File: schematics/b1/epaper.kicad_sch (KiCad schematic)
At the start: 0 parts

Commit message: Added schematic page for the status block.
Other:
- company: (none) -> shawnd.xyz
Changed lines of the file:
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@@
   (title_block
     (title "B1")
-    (date "2024-02-01")
+    (date "2024-02-05")
     (rev "1")
+    (company "shawnd.xyz")
     (comment 2 "scanning as well as radio communications and outputs/displays.")
     (comment 3 "A B1 (Badger One) node is the core hardware unit of the Badger sytem. It handles card")

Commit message: Added schematic page for e-paper block.
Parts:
- added C15: 10u, symbol Device:C_Polarized
- added C16: 1u, symbol Device:C
- added C17: 0.1u, symbol Device:C
- added U5: ~, symbol custom:E-paper_Display
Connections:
- new net BUSY: U5.1 (BUSY)
- new net CLK: U5.5 (CLK)
- new net CS: U5.4 (CS)
- new net DC: U5.3 (DC)
- new net DIN: U5.6 (DIN)
- new net GND: C15.2, C16.2, C17.2, U5.7 (GND)
- new net RST: U5.2 (RST)
- new net VCC: C15.1, C16.1, C17.1, U5.8 (VCC)
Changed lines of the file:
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@@
 (kicad_sch (version 20230121) (generator eeschema)
-  (paper "A4")
+  (paper "A5")
   (title_block
     (title "B1")
@@
     (rev "1")
     (company "shawnd.xyz")
-    (comment 2 "scanning as well as radio communications and outputs/displays.")
-    (comment 3 "A B1 (Badger One) node is the core hardware unit of the Badger sytem. It handles card")
+    (comment 3 "for text, images, or shapes.")
+    (comment 4 "The e-paper block is just a Waveshare 2.9-inch e-paper module that provides a display")
+  )
+  (junction (at 78.74 40.64) (diameter 0) (color 0 0 0 0)
+  )
+  (junction (at 66.04 50.8) (diameter 0) (color 0 0 0 0)
+  )
+  (junction (at 90.17 40.64) (diameter 0) (color 0 0 0 0)
+  )
+  (junction (at 104.14 40.64) (diameter 0) (color 0 0 0 0)
+  )
+  (junction (at 78.74 50.8) (diameter 0) (color 0 0 0 0)
+  )
+  (wire (pts (xy 90.17 40.64) (xy 90.17 41.91))
+    (stroke (width 0) (type default))
+  )
+  (wire (pts (xy 66.04 52.07) (xy 66.04 50.8))
+    (stroke (width 0) (type default))
+  )
+  (wire (pts (xy 78.74 50.8) (xy 78.74 49.53))
+    (stroke (width 0) (type default))
+  )
+  (wire (pts (xy 78.74 40.64) (xy 78.74 41.91))
+    (stroke (width 0) (type default))
+  )
+  (wire (pts (xy 66.04 49.53) (xy 66.04 50.8))
+    (stroke (width 0) (type default))
+  )
+  (wire (pts (xy 90.17 40.64) (xy 78.74 40.64))
+    (stroke (width 0) (type default))
+  )
+  (wire (pts (xy 104.14 50.8) (xy 104.14 40.64))
+    (stroke (width 0) (type default))
+  )
+  (wire (pts (xy 90.17 40.64) (xy 104.14 40.64))
+    (stroke (width 0) (type default))
+  )
+  (wire (pts (xy 104.14 39.37) (xy 104.14 40.64))
+    (stroke (width 0) (type default))
+  )
+  (wire (pts (xy 90.17 50.8) (xy 90.17 49.53))
+    (stroke (width 0) (type default))
+  )
+  (wire (pts (xy 66.04 41.91) (xy 66.04 40.64))
+    (stroke (width 0) (type default))
+  )
+  (wire (pts (xy 66.04 40.64) (xy 78.74 40.64))
+    (stroke (width 0) (type default))
+  )
+  (wire (pts (xy 78.74 50.8) (xy 90.17 50.8))
+    (stroke (width 0) (type default))
+  )
+  (wire (pts (xy 66.04 50.8) (xy 78.74 50.8))
+    (stroke (width 0) (type default))
+  )
+  (hierarchical_label "RST" (shape input) (at 93.98 58.42 180) (fields_autoplaced)
+    (effects (font (size 1.27 1.27)) (justify right))
+  )
+  (hierarchical_label "CLK" (shape input) (at 93.98 66.04 180) (fields_autoplaced)
+    (effects (font (size 1.27 1.27)) (justify right))
+  )
+  (hierarchical_label "DIN" (shape input) (at 93.98 68.58 180) (fields_autoplaced)
+    (effects (font (size 1.27 1.27)) (justify right))
+  )
+  (hierarchical_label "DC" (shape input) (at 93.98 60.96 180) (fields_autoplaced)
+    (effects (font (size 1.27 1.27)) (justify right))
+  )
+  (hierarchical_label "CS" (shape input) (at 93.98 63.5 180) (fields_autoplaced)
+    (effects (font (size 1.27 1.27)) (justify right))
+  )
+  (hierarchical_label "BUSY" (shape output) (at 114.3 58.42 0) (fields_autoplaced)
+    (effects (font (size 1.27 1.27)) (justify left))
+  )
+  (hierarchical_label "VCC" (shape input) (at 104.14 39.37 90) (fields_autoplaced)
+    (effects (font (size 1.27 1.27)) (justify left))
+  )
+  (symbol (lib_id "Device:C") (at 78.74 45.72 0) (unit 1)
+    (in_bom yes) (on_board yes) (dnp no) (fields_autoplaced)
+    (property "Reference" "C16" (at 82.55 44.45 0)
+      (effects (font (size 1.27 1.27)) (justify left))
+    )
+    (property "Value" "1u" (at 82.55 46.99 0)
+      (effects (font (size 1.27 1.27)) (justify left))
+    )
+    (property "Footprint" "" (at 79.7052 49.53 0)
+      (effects (font (size 1.27 1.27)) hide)
+    )
+    (property "Datasheet" "~" (at 78.74 45.72 0)
+      (effects (font (size 1.27 1.27)) hide)
+    )
+    (pin "2")
+    (pin "1")
+    (instances
+      (project "b1"
+        (path "/d6142fa5-2354-4512-9919-37616259c364/793d8791-3733-41a0-9e62-38f7f458300f"
+          (reference "C16") (unit 1)
+        )
+      )
+    )
+  )
+  (symbol (lib_id "Device:C_Polarized") (at 66.04 45.72 0) (unit 1)
+    (in_bom yes) (on_board yes) (dnp no)
+    (property "Reference" "C15" (at 69.85 44.45 0)
+      (effects (font (size 1.27 1.27)) (justify left))
+    )
+    (property "Value" "10u" (at 69.85 46.99 0)
+      (effects (font (size 1.27 1.27)) (justify left))
+    )
+    (property "Footprint" "" (at 67.0052 49.53 0)
+      (effects (font (size 1.27 1.27)) hide)
+    )
+    (property "Datasheet" "~" (at 66.04 45.72 0)
+      (effects (font (size 1.27 1.27)) hide)
+    )
+    (pin "2")
+    (pin "1")
+    (instances
+      (project "b1"
+        (path "/d6142fa5-2354-4512-9919-37616259c364/793d8791-3733-41a0-9e62-38f7f458300f"
+          (reference "C15") (unit 1)
+        )
+      )
+    )
+  )
+  (symbol (lib_id "power:GND") (at 66.04 52.07 0) (unit 1)
+    (in_bom yes) (on_board yes) (dnp no) (fields_autoplaced)
+    (property "Reference" "#PWR024" (at 66.04 58.42 0)
+      (effects (font (size 1.27 1.27)) hide)
+    )
+    (property "Value" "GND" (at 66.04 57.15 0)
+      (effects (font (size 1.27 1.27)))
+    )
+    (property "Footprint" "" (at 66.04 52.07 0)
+      (effects (font (size 1.27 1.27)) hide)
+    )
+    (property "Datasheet" "" (at 66.04 52.07 0)
+      (effects (font (size 1.27 1.27)) hide)
+    )
+    (pin "1")
+    (instances
+      (project "b1"
+        (path "/d6142fa5-2354-4512-9919-37616259c364/793d8791-3733-41a0-9e62-38f7f458300f"
+          (reference "#PWR024") (unit 1)
+        )
+      )
+    )
+  )
+  (symbol (lib_id "power:GND") (at 104.14 76.2 0) (unit 1)
+    (in_bom yes) (on_board yes) (dnp no) (fields_autoplaced)
+    (property "Reference" "#PWR025" (at 104.14 82.55 0)
+      (effects (font (size 1.27 1.27)) hide)
+    )
+    (property "Value" "GND" (at 104.14 81.28 0)
+      (effects (font (size 1.27 1.27)))
+    )
+    (property "Footprint" "" (at 104.14 76.2 0)
+      (effects (font (size 1.27 1.27)) hide)
+    )
+    (property "Datasheet" "" (at 104.14 76.2 0)
+      (effects (font (size 1.27 1.27)) hide)
+    )
+    (pin "1")
+    (instances
+      (project "b1"
+        (path "/d6142fa5-2354-4512-9919-37616259c364/793d8791-3733-41a0-9e62-38f7f458300f"
+          (reference "#PWR025") (unit 1)
+        )
+      )
+    )
+  )
+  (symbol (lib_id "Device:C") (at 90.17 45.72 0) (unit 1)
+    (in_bom yes) (on_board yes) (dnp no)
+    (property "Reference" "C17" (at 93.98 44.45 0)
+      (effects (font (size 1.27 1.27)) (justify left))
+    )
+    (property "Value" "0.1u" (at 93.98 46.99 0)
+      (effects (font (size 1.27 1.27)) (justify left))
+    )
+    (property "Footprint" "" (at 91.1352 49.53 0)
+      (effects (font (size 1.27 1.27)) hide)
+    )
+    (property "Datasheet" "~" (at 90.17 45.72 0)
+      (effects (font (size 1.27 1.27)) hide)
+    )
+    (pin "2")
+    (pin "1")
+    (instances
+      (project "b1"
+        (path "/d6142fa5-2354-4512-9919-37616259c364/793d8791-3733-41a0-9e62-38f7f458300f"
+          (reference "C17") (unit 1)
+        )
+      )
+    )
+  )
+  (symbol (lib_id "custom:E-paper_Display") (at 104.14 58.42 0) (unit 1)
+    (in_bom yes) (on_board yes) (dnp no)
+    (property "Reference" "U5" (at 106.68 49.53 0)
+      (effects (font (size 1.27 1.27)))
+    )
+    (property "Value" "~" (at 104.14 50.8 0)
+      (effects (font (size 1.27 1.27)))
+    )
+    (property "Footprint" "" (at 104.14 50.8 0)
+      (effects (font (size 1.27 1.27)) hide)
+    )
+    (property "Datasheet" "" (at 104.14 50.8 0)
+      (effects (font (size 1.27 1.27)) hide)
+    )
+    (pin "7")
+    (pin "5")
+    (pin "3")
+    (pin "6")
+    (pin "2")
+    (pin "4")
+    (pin "1")
+    (pin "8")
+    (instances
+      (project "b1"
+        (path "/d6142fa5-2354-4512-9919-37616259c364/793d8791-3733-41a0-9e62-38f7f458300f"
+          (reference "U5") (unit 1)
+        )
+      )
+    )
   )
 )

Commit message: Updated labels.
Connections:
- net CS renamed ~{CS}
- net RST renamed ~{RST}
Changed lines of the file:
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@@
     (stroke (width 0) (type default))
   )
-  (hierarchical_label "RST" (shape input) (at 93.98 58.42 180) (fields_autoplaced)
+  (hierarchical_label "~{RST}" (shape input) (at 93.98 58.42 180) (fields_autoplaced)
     (effects (font (size 1.27 1.27)) (justify right))
   )
@@
     (effects (font (size 1.27 1.27)) (justify right))
   )
-  (hierarchical_label "CS" (shape input) (at 93.98 63.5 180) (fields_autoplaced)
+  (hierarchical_label "~{CS}" (shape input) (at 93.98 63.5 180) (fields_autoplaced)
     (effects (font (size 1.27 1.27)) (justify right))
   )

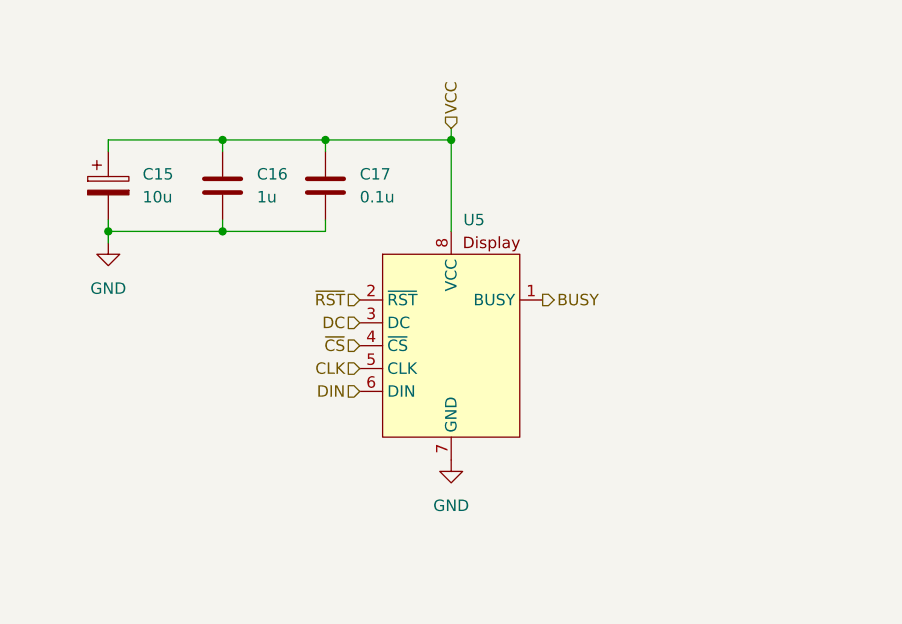
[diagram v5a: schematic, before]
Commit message: Updated e-paper block schematic.
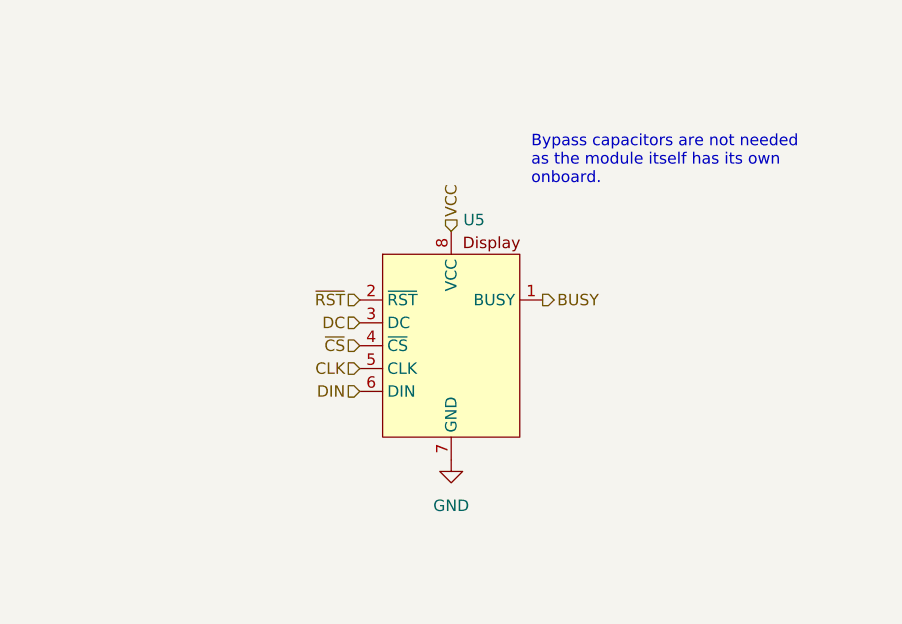
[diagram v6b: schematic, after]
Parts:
- removed C15: 10u, symbol Device:C_Polarized
- removed C16: 1u, symbol Device:C
- removed C17: 0.1u, symbol Device:C
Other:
- note added: "Bypass capacitors are not needed as the module itself has its own onboard."
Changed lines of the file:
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@@
     (comment 4 "The e-paper block is just a Waveshare 2.9-inch e-paper module that provides a display")
   )
-  (junction (at 78.74 40.64) (diameter 0) (color 0 0 0 0)
-  )
-  (junction (at 66.04 50.8) (diameter 0) (color 0 0 0 0)
-  )
-  (junction (at 90.17 40.64) (diameter 0) (color 0 0 0 0)
-  )
-  (junction (at 104.14 40.64) (diameter 0) (color 0 0 0 0)
-  )
-  (junction (at 78.74 50.8) (diameter 0) (color 0 0 0 0)
-  )
-  (wire (pts (xy 90.17 40.64) (xy 90.17 41.91))
-    (stroke (width 0) (type default))
-  )
-  (wire (pts (xy 66.04 52.07) (xy 66.04 50.8))
-    (stroke (width 0) (type default))
-  )
-  (wire (pts (xy 78.74 50.8) (xy 78.74 49.53))
-    (stroke (width 0) (type default))
-  )
-  (wire (pts (xy 78.74 40.64) (xy 78.74 41.91))
-    (stroke (width 0) (type default))
-  )
-  (wire (pts (xy 66.04 49.53) (xy 66.04 50.8))
-    (stroke (width 0) (type default))
-  )
-  (wire (pts (xy 90.17 40.64) (xy 78.74 40.64))
-    (stroke (width 0) (type default))
-  )
-  (wire (pts (xy 104.14 50.8) (xy 104.14 40.64))
-    (stroke (width 0) (type default))
-  )
-  (wire (pts (xy 90.17 40.64) (xy 104.14 40.64))
-    (stroke (width 0) (type default))
-  )
-  (wire (pts (xy 104.14 39.37) (xy 104.14 40.64))
-    (stroke (width 0) (type default))
-  )
-  (wire (pts (xy 90.17 50.8) (xy 90.17 49.53))
-    (stroke (width 0) (type default))
-  )
-  (wire (pts (xy 66.04 41.91) (xy 66.04 40.64))
-    (stroke (width 0) (type default))
-  )
-  (wire (pts (xy 66.04 40.64) (xy 78.74 40.64))
-    (stroke (width 0) (type default))
-  )
-  (wire (pts (xy 78.74 50.8) (xy 90.17 50.8))
-    (stroke (width 0) (type default))
-  )
-  (wire (pts (xy 66.04 50.8) (xy 78.74 50.8))
-    (stroke (width 0) (type default))
+  (text "Bypass capacitors are not needed\nas the module itself has its own\nonboard."
+    (at 113.03 45.72 0)
+    (effects (font (size 1.27 1.27)) (justify left bottom))
   )
   (hierarchical_label "~{RST}" (shape input) (at 93.98 58.42 180) (fields_autoplaced)
@@
     (effects (font (size 1.27 1.27)) (justify left))
   )
-  (hierarchical_label "VCC" (shape input) (at 104.14 39.37 90) (fields_autoplaced)
+  (hierarchical_label "VCC" (shape input) (at 104.14 50.8 90) (fields_autoplaced)
     (effects (font (size 1.27 1.27)) (justify left))
-  )
-  (symbol (lib_id "Device:C") (at 78.74 45.72 0) (unit 1)
-    (in_bom yes) (on_board yes) (dnp no) (fields_autoplaced)
-    (property "Reference" "C16" (at 82.55 44.45 0)
-      (effects (font (size 1.27 1.27)) (justify left))
-    )
-    (property "Value" "1u" (at 82.55 46.99 0)
-      (effects (font (size 1.27 1.27)) (justify left))
-    )
-    (property "Footprint" "" (at 79.7052 49.53 0)
-      (effects (font (size 1.27 1.27)) hide)
-    )
-    (property "Datasheet" "~" (at 78.74 45.72 0)
-      (effects (font (size 1.27 1.27)) hide)
-    )
-    (pin "2")
-    (pin "1")
-    (instances
-      (project "b1"
-        (path "/d6142fa5-2354-4512-9919-37616259c364/793d8791-3733-41a0-9e62-38f7f458300f"
-          (reference "C16") (unit 1)
-        )
-      )
-    )
-  )
-  (symbol (lib_id "Device:C_Polarized") (at 66.04 45.72 0) (unit 1)
-    (in_bom yes) (on_board yes) (dnp no)
-    (property "Reference" "C15" (at 69.85 44.45 0)
-      (effects (font (size 1.27 1.27)) (justify left))
-    )
-    (property "Value" "10u" (at 69.85 46.99 0)
-      (effects (font (size 1.27 1.27)) (justify left))
-    )
-    (property "Footprint" "" (at 67.0052 49.53 0)
-      (effects (font (size 1.27 1.27)) hide)
-    )
-    (property "Datasheet" "~" (at 66.04 45.72 0)
-      (effects (font (size 1.27 1.27)) hide)
-    )
-    (pin "2")
-    (pin "1")
-    (instances
-      (project "b1"
-        (path "/d6142fa5-2354-4512-9919-37616259c364/793d8791-3733-41a0-9e62-38f7f458300f"
-          (reference "C15") (unit 1)
-        )
-      )
-    )
-  )
-  (symbol (lib_id "power:GND") (at 66.04 52.07 0) (unit 1)
-    (in_bom yes) (on_board yes) (dnp no) (fields_autoplaced)
-    (property "Reference" "#PWR03" (at 66.04 58.42 0)
-      (effects (font (size 1.27 1.27)) hide)
-    )
-    (property "Value" "GND" (at 66.04 57.15 0)
-      (effects (font (size 1.27 1.27)))
-    )
-    (property "Footprint" "" (at 66.04 52.07 0)
-      (effects (font (size 1.27 1.27)) hide)
-    )
-    (property "Datasheet" "" (at 66.04 52.07 0)
-      (effects (font (size 1.27 1.27)) hide)
-    )
-    (pin "1")
-    (instances
-      (project "b1"
-        (path "/d6142fa5-2354-4512-9919-37616259c364/793d8791-3733-41a0-9e62-38f7f458300f"
-          (reference "#PWR03") (unit 1)
-        )
-      )
-    )
   )
   (symbol (lib_id "power:GND") (at 104.14 76.2 0) (unit 1)
@@
         )
       )
-    )
-  )
-  (symbol (lib_id "Device:C") (at 90.17 45.72 0) (unit 1)
-    (in_bom yes) (on_board yes) (dnp no)
-    (property "Reference" "C17" (at 93.98 44.45 0)
-      (effects (font (size 1.27 1.27)) (justify left))
-    )
-    (property "Value" "0.1u" (at 93.98 46.99 0)
-      (effects (font (size 1.27 1.27)) (justify left))
-    )
-    (property "Footprint" "" (at 91.1352 49.53 0)
-      (effects (font (size 1.27 1.27)) hide)
-    )
-    (property "Datasheet" "~" (at 90.17 45.72 0)
-      (effects (font (size 1.27 1.27)) hide)
-    )
-    (pin "2")
-    (pin "1")
-    (instances
-      (project "b1"
-        (path "/d6142fa5-2354-4512-9919-37616259c364/793d8791-3733-41a0-9e62-38f7f458300f"
-          (reference "C17") (unit 1)
-        )
-      )

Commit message: Updated annotations.
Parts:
- renumbered U5 to U6
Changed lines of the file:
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@@
   (title_block
     (title "B1")
-    (date "2024-02-06")
+    (date "2024-02-15")
     (rev "1")
     (company "shawnd.xyz")
@@
   (symbol (lib_id "power:GND") (at 104.14 76.2 0) (unit 1)
     (in_bom yes) (on_board yes) (dnp no) (fields_autoplaced)
-    (property "Reference" "#PWR04" (at 104.14 82.55 0)
+    (property "Reference" "#PWR021" (at 104.14 82.55 0)
       (effects (font (size 1.27 1.27)) hide)
     )
@@
       (project "b1"
         (path "/d6142fa5-2354-4512-9919-37616259c364/793d8791-3733-41a0-9e62-38f7f458300f"
-          (reference "#PWR04") (unit 1)
+          (reference "#PWR021") (unit 1)
         )
       )
@@
   (symbol (lib_id "custom:E-paper_Display") (at 104.14 58.42 0) (unit 1)
     (in_bom yes) (on_board yes) (dnp no)
-    (property "Reference" "U5" (at 106.68 49.53 0)
+    (property "Reference" "U6" (at 106.68 49.53 0)
       (effects (font (size 1.27 1.27)))
     )
@@
       (project "b1"
         (path "/d6142fa5-2354-4512-9919-37616259c364/793d8791-3733-41a0-9e62-38f7f458300f"
-          (reference "U5") (unit 1)
+          (reference "U6") (unit 1)
         )
       )

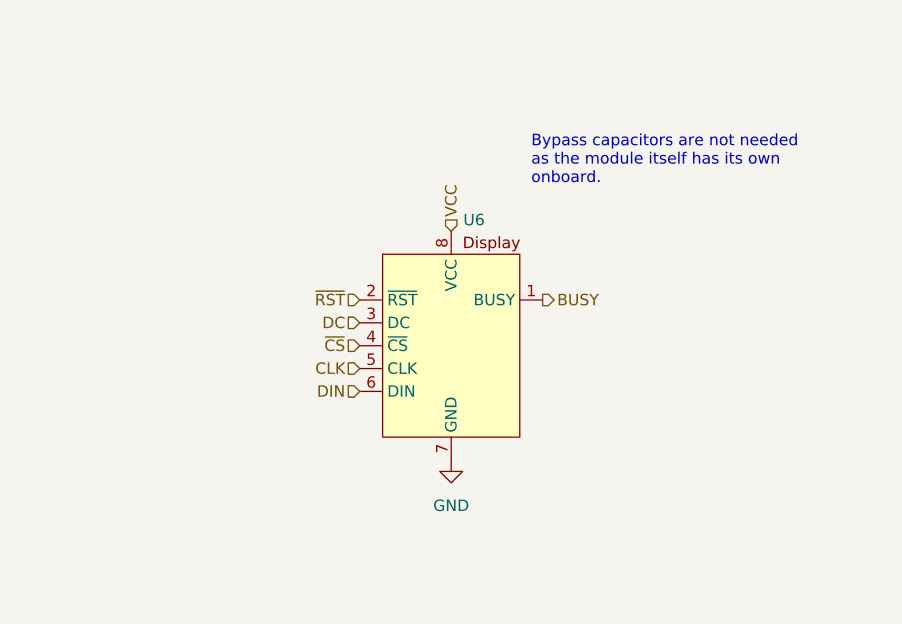
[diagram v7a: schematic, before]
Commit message: Wired the e-paper display.
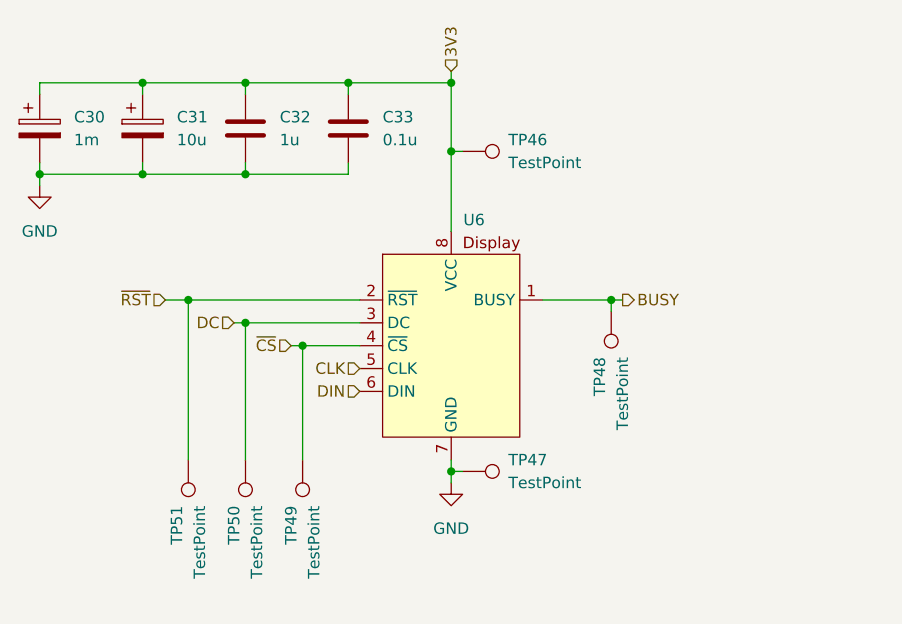
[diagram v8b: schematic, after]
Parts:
- added C30: 1m, symbol Device:C_Polarized
- added C31: 10u, symbol Device:C_Polarized
- added C32: 1u, symbol Device:C
- added C33: 0.1u, symbol Device:C
- added TP46, TP47, TP48, TP49, TP50, TP51: TestPoint, symbol Connector:TestPoint
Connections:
- net BUSY: now also TP48.1
- net DC: now also TP50.1
- net GND: now also C30.2, C31.2, C32.2, C33.2, TP47.1
- net ~{CS}: now also TP49.1
- net ~{RST}: now also TP51.1
- net VCC renamed 3V3
- net 3V3: now also C30.1, C31.1, C32.1, C33.1, TP46.1
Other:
- note removed: "Bypass capacitors are not needed as the module itself has its own onboard."
